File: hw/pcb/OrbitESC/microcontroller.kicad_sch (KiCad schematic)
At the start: 11 parts, among them J2 Micro_SD_Card_Det, J6 CAN1, J7 Serial1, SW1 Reset, SW2 Boot, SW3 Break, U1 MCP2551-I-SN, U2 AT25SF081-SSHD-X, U3 24LC128, U4 STM32F446ZCHx, X1 ECS-2520MV-240-BN

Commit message: Fill out majority of schematic
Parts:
- removed SW1: Reset, Button_Switch_SMD:SW_SPST_PTS810, symbol Switch:SW_Push
- removed SW2: Boot, Button_Switch_SMD:SW_SPST_PTS810, symbol Switch:SW_Push
- removed SW3: Break, Button_Switch_SMD:SW_SPST_PTS810, symbol Switch:SW_Push
- removed U1: MCP2551-I-SN, Package_SO:SOIC-8_3.9x4.9mm_P1.27mm, symbol Interface_CAN_LIN:MCP2551-I-SN
- added C33, C37, C38, C53: 2.2uF, Capacitor_SMD:C_0805_2012Metric, symbol Device:C
- added C34, C35, C36, C39, C40, C41, C42, C43, C44, C45, C46, C47, C48, C49, C50, C51, C52, C54, C55, C56: 100nF, Capacitor_SMD:C_0402_1005Metric, symbol Device:C
- added D10, D11, D8, D9: Yellow LED, Diode_SMD:D_0603_1608Metric, symbol Device:LED
- added D12, D13, D6, D7: 3.3V, Diode_SMD:D_MiniMELF, symbol Device:D_Zener
- added J10: ~, Connector_PinHeader_1.27mm:PinHeader_2x05_P1.27mm_Vertical, symbol Connector_Generic:Conn_02x05_Odd_Even
- added J8: Serial2, Connector_JST:JST_PH_B3B-PH-K_1x03_P2.00mm_Vertical, symbol Connector:Conn_01x03_Male
- added J9: CAN2, Connector_JST:JST_PH_B3B-PH-K_1x03_P2.00mm_Vertical, symbol Connector:Conn_01x03_Male
- added R58, R59, R60, R61, R64, R65, R66, R67, R68, R77, R78: 1.5k, Resistor_SMD:R_0402_1005Metric, symbol Device:R_US
- added R62, R63: 120, Resistor_SMD:R_0402_1005Metric, symbol Device:R_US
- added R69, R70, R71: 10k, Resistor_SMD:R_0402_1005Metric, symbol Device:R_US
- added R72, R73, R74, R75, R76: 39k, Resistor_SMD:R_0402_1005Metric, symbol Device:R_US
- added R80, R81, R82, R83: 100k, Resistor_SMD:R_0402_1005Metric, symbol Device:R_US
- added TP?: SDIO_CMD, TestPoint:TestPoint_Pad_D1.0mm, symbol Connector:TestPoint_Small
- added TP? (x2): TestPoint_Small, TestPoint:TestPoint_Pad_D1.0mm, symbol Connector:TestPoint_Small
- added U1, U10: TLE9250X, Package_SON:HVSON-8-1EP_3x3mm_P0.65mm_EP1.6x2.4mm, symbol CANTransciever:TLE9250X
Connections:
- net +3.3V: now also J2.4 (VDD), U2.3 (~{WP}/IO2), U2.7 (~{HOLD}/IO3), U2.8 (VCC), U3.8 (VCC), U4.C11 (VDDUSB), U4.C2 (VBAT), U4.D3 (VDD), U4.E5 (PDR_ON), U4.F10 (VDD), U4.F4 (VDD), U4.F5 (VDD), U4.F6 (VDD), U4.F7 (VDD), U4.F8 (VDD), U4.F9 (VDD), U4.G5 (VDD), U4.G6 (VDD), U4.G7 (VDD), X1.4 (VDD), C33.2, C34.2, C35.2, C36.2, C39.2, C40.2, C41.2, C42.2, C43.2, C44.2, C45.2, C46.2, C47.2, C48.2, C50.2, C51.2, C52.2, C53.2, C54.2, C55.2, C56.2, R64.2, R70.2, R71.2, R72.1, R73.1, R74.1, R75.1, R76.1, R77.2, R78.1, U1.5 (VIO), U10.5 (VIO)
- net +3.3VADC: now also U4.L1 (VREF+), U4.M1 (VDDA)
- net +5V: now also U1.3 (VCC), U10.3 (VCC)
- net USB_ENUM: now also U4.E12 (PA8); no longer U4.F12 (PC7)
- net GND: now reaches X1.2 (GND)
- net GND: now also J2.11 (SHIELD), J2.6 (VSS), J2.9 (DET_B), J6.2 (Pin_2), J7.3 (Pin_3), U2.4 (GND), U3.1 (A0), U3.2 (A1), U3.3 (A2), U3.4 (GND), U3.7 (WP), U4.D2 (VSS), U4.E6 (VSS), U4.E7 (VSS), U4.G10 (VSS), U4.G4 (VSS), U4.G8 (VSS), U4.H6 (VSS), U4.J1 (VSSA), U4.K1 (VREF-), C33.1, C34.1, C35.1, C36.1, C37.1, C38.1, C39.1, C40.1, C41.1, C42.1, C43.1, C44.1, C45.1, C46.1, C47.1, C48.1, C49.1, C50.1, C51.1, C52.1, C53.1, C54.1, C55.1, C56.1, D10.1 (K), D11.1 (K), D12.2 (A), D13.2 (A), D6.2 (A), D7.2 (A), D8.1 (K), D9.1 (K), J10.3 (Pin_3), J10.5 (Pin_5), J10.9 (Pin_9), J8.3 (Pin_3), J9.2 (Pin_2), R69.1, R80.1, R81.1, R82.2, R83.2, U1.2 (GND), U1.9 (PAD), U10.2 (GND), U10.9 (PAD)
- net OSC: now reaches X1.3 (OUT)
- net OSC: now also U4.D1 (PH0)
- net SDIO_DATA_2: now reaches J2.1 (DAT2)
- net SDIO_DATA_2: now also U4.B11 (PC10), R76.2
- net SDIO_CARD_DETECT: now reaches J2.10 (DET_A)
- net SDIO_CARD_DETECT: now also U4.D10 (PD1), C49.2, R72.2
- net SDIO_DATA_3: now reaches J2.2 (DAT3/CD)
- net SDIO_DATA_3: now also U4.B10 (PC11), R75.2
- net SDIO_CMD: now reaches J2.3 (CMD)
- net SDIO_CMD: now also U4.E9 (PD2), R71.1, TP?.1
- net SDIO_CLK: now reaches J2.5 (CLK)
- net SDIO_CLK: now also U4.C10 (PC12), TP?.1
- net SDIO_DATA_0: now reaches J2.7 (DAT0)
- net SDIO_DATA_0: now also U4.F11 (PC8), R73.2
- net SDIO_DATA_1: now reaches J2.8 (DAT1)
- net SDIO_DATA_1: now also U4.E11 (PC9), R74.2
- net HEARTBEAT_LED: now reaches U4.A1 (PC13)
- net JTAG_TDI: now reaches U4.A10 (PA15)
- net JTAG_TDI: now also J10.8 (Pin_8)
- net JTAG_TCLK: now reaches U4.A11 (PA14)
- net JTAG_TCLK: now also J10.4 (Pin_4)
- net JTAG_TMS: now reaches U4.A12 (PA13)
- net JTAG_TMS: now also J10.2 (Pin_2)
- net USER_BTN: now reaches U4.A2 (PE3)
- net ARMED_LED: now reaches U4.A4 (PE1)
- net CAN1_ACTV_LED: now reaches U4.A5 (PE0)
- net CAN1_ACTV_LED: now also R65.1
- net JTAG_TDO: now reaches U4.A7 (PB3)
- net JTAG_TDO: now also J10.6 (Pin_6)
- net SERIAL1_IN: now reaches U4.A8 (PD6)
- net SERIAL1_IN: now also R58.1, R82.1
- net STATUS_0_LED: now reaches U4.B2 (PE4)
- net STATUS_1_LED: now reaches U4.B3 (PE5)
- net STATUS_2_LED: now reaches U4.B4 (PE6)
- net CAN1_TXD: now reaches U4.B5 (PB9)
- net CAN1_TXD: now also U1.1 (TxD)
- net CAN2_RXD: now reaches U4.B6 (PB5)
- net CAN2_RXD: now also U10.4 (RxD)
- net CAN2_ACTV_LED: now reaches U4.B7 (PG15)
- net CAN2_ACTV_LED: now also R66.1
- net SERIAL1_ACTV_LED: now reaches U4.B8 (PG12)
- net SERIAL1_ACTV_LED: now also R67.1
- net SERIAL1_OUT: now reaches U4.B9 (PD5)
- net SERIAL1_OUT: now also R60.1, R80.2
- net EEPROM_SDA: now reaches U4.C3 (PF0)
- net EEPROM_SDA: now also U3.5 (SDA), R77.1
- net EEPROM_SCL: now reaches U4.C4 (PF1)
- net EEPROM_SCL: now also U3.6 (SCL), R78.2
- net CAN1_RXD: now reaches U4.C5 (PB8)
- net CAN1_RXD: now also U1.4 (RxD)
- net CAN2_TXD: now reaches U4.C6 (PB6)
- net CAN2_TXD: now also U10.1 (TxD)
- net SERIAL2_OUT: now reaches U4.C7 (PG14)
- net SERIAL2_OUT: now also R61.1, R81.2
- net USB_ACTV_LED: now reaches U4.D11 (PA10)
- net BOOT0: now reaches U4.D5 (BOOT0)
- net SERIAL2_ACTV_LED: now reaches U4.D7 (PG13)
- net SERIAL2_ACTV_LED: now also R68.1
- net TEMP_VA: now reaches U4.E2 (PF3)
- net SERIAL2_IN: now reaches U4.E8 (PG9)
- net SERIAL2_IN: now also R59.1, R83.1
- net nRESET: now reaches U4.F1 (NRST)
- net nRESET: now also J10.10 (Pin_10)
- net +3V3_VOLTAGE: now reaches U4.G1 (PF10)
- net TEMP_VB: now reaches U4.G2 (PF9)
- net at U4.G9 (VCAP_2): now also C38.2
- net +5V0_VOLTAGE: now reaches U4.H1 (PC0)
- net at U4.H5 (BYPASS_REG): now also R69.2
- net at U4.H7 (VCAP_1): now also C37.2
- net GATE_DRIVE_BH: now reaches U4.H8 (PE11)
- net INPUT_VOLTAGE: now reaches U4.J2 (PA0)
- net MOTOR_VA: now reaches U4.J3 (PA4)
- net BOOT1: now reaches U4.J5 (PB2)
- net GATE_DRIVE_BL: now reaches U4.J7 (PE10)
- net GATE_DRIVE_CL: now reaches U4.J8 (PE12)
- net MOTOR_IA: now reaches U4.K2 (PA1)
- net MOTOR_VB: now reaches U4.K3 (PA5)
- net GATE_DRIVE_AH: now reaches U4.K7 (PE9)
- net GATE_DRIVE_CH: now reaches U4.K8 (PE13)
- net NOR_MISO: now reaches U4.L11 (PB14)
- net NOR_MISO: now also U2.2 (SO/IO1)
- net NOR_MOSI: now reaches U4.L12 (PB15)
- net NOR_MOSI: now also U2.5 (SI/IO0)
- net MOTOR_IB: now reaches U4.L2 (PA2)
- net MOTOR_VC: now reaches U4.L3 (PA6)
- net GATE_DRIVE_AL: now reaches U4.L7 (PE8)
- net NOR_nCS: now reaches U4.M11 (PB12)
- net NOR_nCS: now also U2.1 (~{CS}), R70.1
- net NOR_SCK: now reaches U4.M12 (PB13)
- net NOR_SCK: now also U2.6 (SCK)
- net MOTOR_IC: now reaches U4.M2 (PA3)
- net TIM1_BREAK: now reaches U4.M8 (PE15)
- net at J7.1 (Pin_1): now also D6.1 (K), R60.2
- net at J7.2 (Pin_2): now also D12.1 (K), R58.2
- net at J6.1 (Pin_1): now also R62.2, U1.7 (CANH)
- net at J6.3 (Pin_3): now also R62.1, U1.6 (CANL)
- new net: J10.1 (Pin_1), R64.1
- new net: D7.1 (K), J8.1 (Pin_1), R61.2
- new net: D13.1 (K), J8.2 (Pin_2), R59.2
- new net: D8.2 (A), R65.2
- new net: D11.2 (A), R68.2
- new net: J9.3 (Pin_3), R63.1, U10.6 (CANL)
- new net: J9.1 (Pin_1), R63.2, U10.7 (CANH)
- new net: D10.2 (A), R67.2
- new net: D9.2 (A), R66.2
- no-connect marks 0 -> 4
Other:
- added sheet InputButton (input_button.kicad_sch)
- added sheet Status LEDs (status_leds.kicad_sch)
- sheet USBCircuitry ports: added ACTV_LED; removed none
- note added: "24MHz Oscillator"
- note added: "Enable Internal Regulator"
- note added: "Join at single point"
- note added: "Power Pins Decoupling"
- note added: "VDDUSB Decoupling"
- moved on the sheet: J2, J6, J7, U2, U3, X1

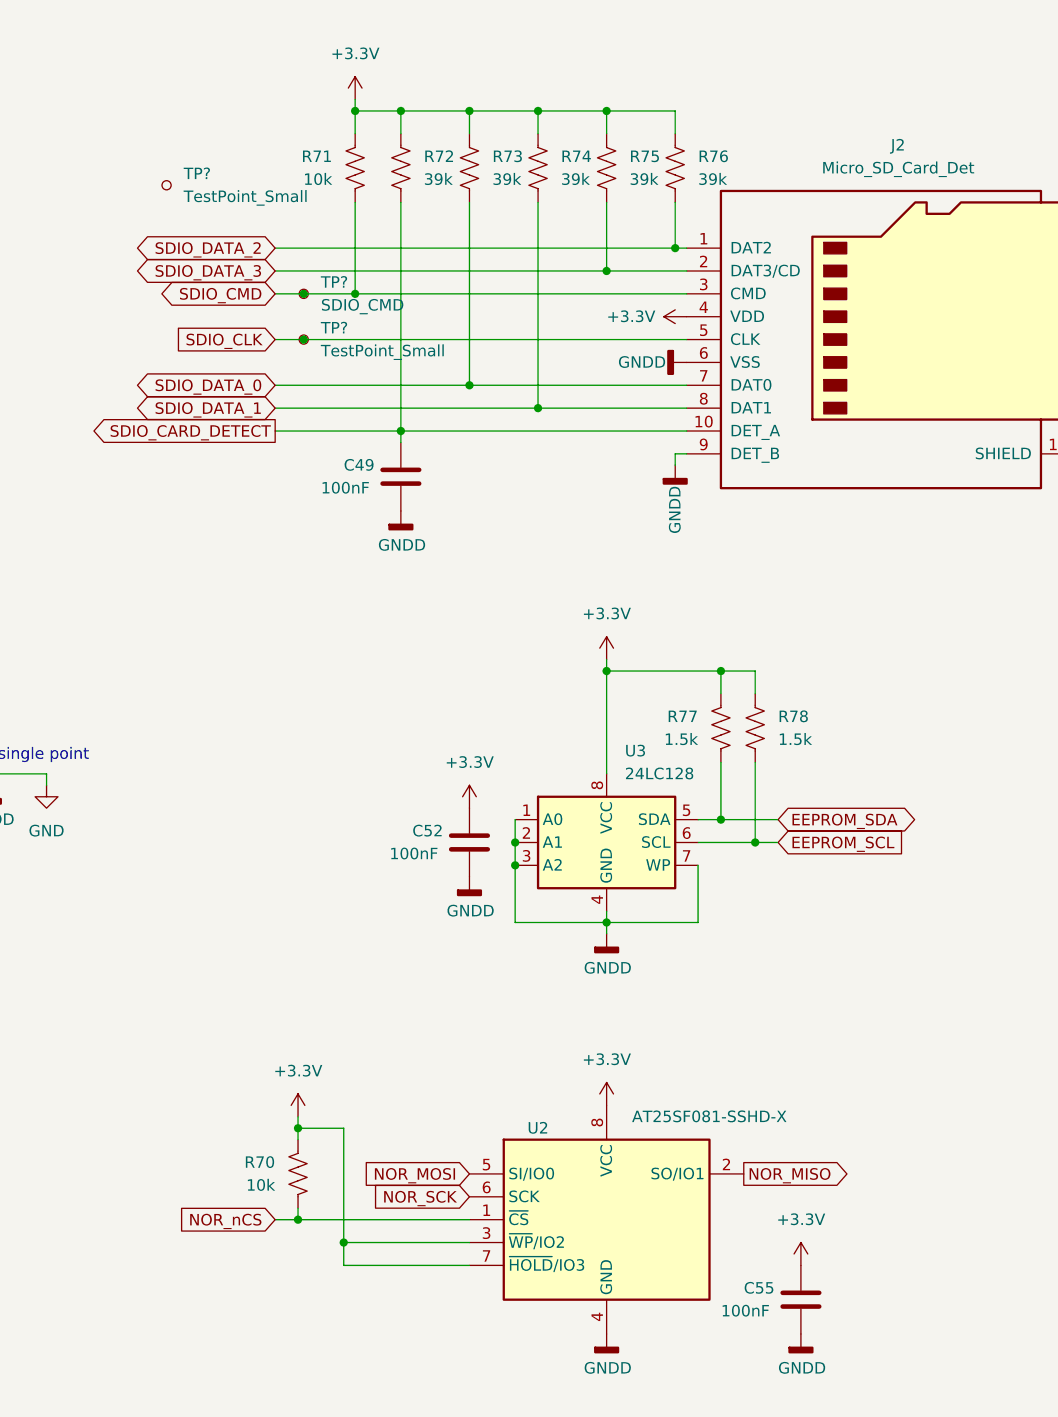
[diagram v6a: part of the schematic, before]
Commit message: Add test pads
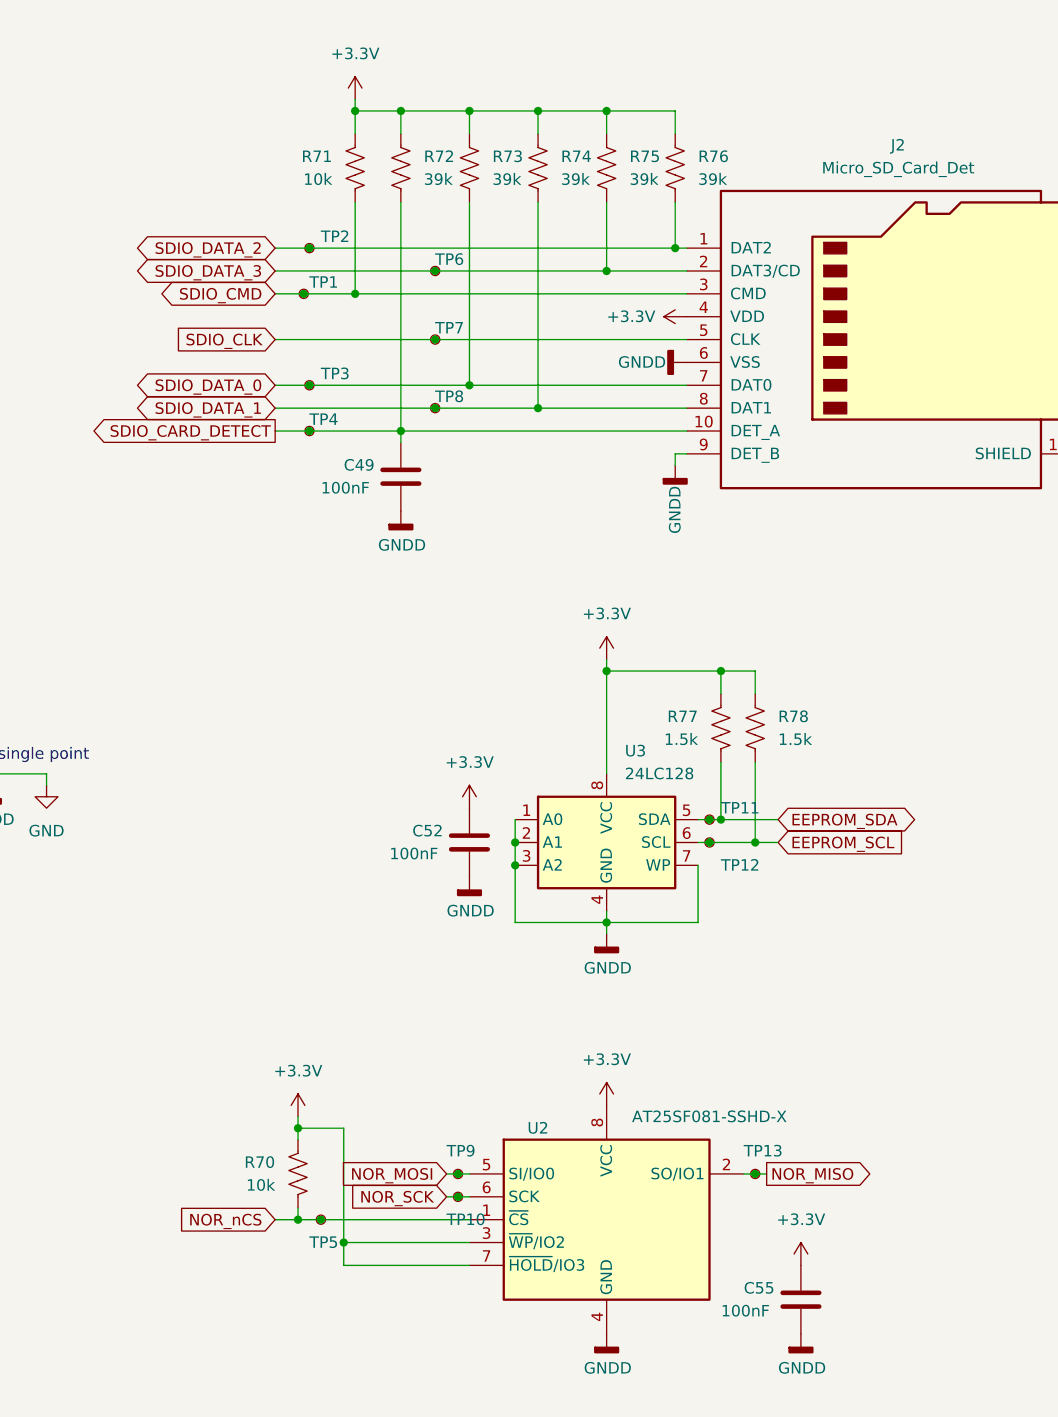
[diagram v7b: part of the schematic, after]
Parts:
- removed TP?: TestPoint_Small, TestPoint:TestPoint_Pad_D1.0mm, symbol Connector:TestPoint_Small
- added TP10: NOR_SCK, TestPoint:TestPoint_Pad_D1.0mm, symbol Connector:TestPoint_Small
- added TP11: EEPROM_SDA, TestPoint:TestPoint_Pad_D1.0mm, symbol Connector:TestPoint_Small
- added TP12: EEPROM_SCL, TestPoint:TestPoint_Pad_D1.0mm, symbol Connector:TestPoint_Small
- added TP13: NOR_MISO, TestPoint:TestPoint_Pad_D1.0mm, symbol Connector:TestPoint_Small
- added TP2: SDIO_DATA_2, TestPoint:TestPoint_Pad_D1.0mm, symbol Connector:TestPoint_Small
- added TP3: SDIO_DATA_0, TestPoint:TestPoint_Pad_D1.0mm, symbol Connector:TestPoint_Small
- added TP4: SDIO_CARD_DETECT, TestPoint:TestPoint_Pad_D1.0mm, symbol Connector:TestPoint_Small
- added TP5: NOR_nCS, TestPoint:TestPoint_Pad_D1.0mm, symbol Connector:TestPoint_Small
- added TP6: SDIO_DATA_3, TestPoint:TestPoint_Pad_D1.0mm, symbol Connector:TestPoint_Small
- added TP8: SDIO_DATA_1, TestPoint:TestPoint_Pad_D1.0mm, symbol Connector:TestPoint_Small
- added TP9: NOR_MOSI, TestPoint:TestPoint_Pad_D1.0mm, symbol Connector:TestPoint_Small
- TP7: renamed from TP?; value TestPoint_Small -> SDIO_CLK
- gave numbers to parts that had none: 1
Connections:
- net EEPROM_SCL: now also TP12.1
- net EEPROM_SDA: now also TP11.1
- net NOR_MISO: now also TP13.1
- net NOR_MOSI: now also TP9.1
- net NOR_SCK: now also TP10.1
- net NOR_nCS: now also TP5.1
- net SDIO_CARD_DETECT: now also TP4.1
- net SDIO_DATA_0: now also TP3.1
- net SDIO_DATA_1: now also TP8.1
- net SDIO_DATA_2: now also TP2.1
- net SDIO_DATA_3: now also TP6.1
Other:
- moved on the sheet: TP7

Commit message: Schematic checklist runthrough
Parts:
- J10: DigiKey (none) -> 609-3712-ND; Digikey 609-3712-ND -> (none); Mouser 649-221111-00010T4LF -> (none)
- J6, J7, J8, J9: DigiKey (none) -> A100035-ND
- U2: DigiKey (none) -> 1265-AT25SF081B-SSHD-B-ND
- U3: DigiKey (none) -> 24LC128T-E/MSCT-ND
- U4: DigiKey (none) -> 497-19011-ND; Digikey 497-19011-ND -> (none)
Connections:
- net FAULT_LED: now also U4.A3 (PE2)
- no-connect marks 4 -> 55
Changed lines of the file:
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@@
   )
   (no_connect (at 232.41 124.46))
+  (no_connect (at 166.37 114.3))
+  (no_connect (at 166.37 134.62))
+  (no_connect (at 166.37 132.08))
+  (no_connect (at 166.37 129.54))
+  (no_connect (at 166.37 139.7))
+  (no_connect (at 166.37 142.24))
+  (no_connect (at 166.37 127))
+  (no_connect (at 166.37 124.46))
+  (no_connect (at 166.37 121.92))
+  (no_connect (at 166.37 119.38))
+  (no_connect (at 166.37 116.84))
+  (no_connect (at 166.37 162.56))
+  (no_connect (at 166.37 167.64))
+  (no_connect (at 166.37 170.18))
+  (no_connect (at 166.37 172.72))
+  (no_connect (at 166.37 175.26))
+  (no_connect (at 166.37 177.8))
+  (no_connect (at 166.37 185.42))
+  (no_connect (at 166.37 187.96))
+  (no_connect (at 166.37 190.5))
   (no_connect (at 109.22 39.37))
+  (no_connect (at 166.37 218.44))
+  (no_connect (at 166.37 236.22))
+  (no_connect (at 232.41 238.76))
+  (no_connect (at 232.41 236.22))
+  (no_connect (at 232.41 233.68))
+  (no_connect (at 232.41 231.14))
+  (no_connect (at 232.41 228.6))
+  (no_connect (at 232.41 226.06))
+  (no_connect (at 232.41 139.7))
+  (no_connect (at 232.41 142.24))
+  (no_connect (at 232.41 132.08))
+  (no_connect (at 232.41 210.82))
+  (no_connect (at 232.41 208.28))
+  (no_connect (at 232.41 200.66))
+  (no_connect (at 232.41 223.52))
+  (no_connect (at 232.41 220.98))
+  (no_connect (at 232.41 218.44))
+  (no_connect (at 232.41 195.58))
+  (no_connect (at 232.41 193.04))
+  (no_connect (at 232.41 175.26))
+  (no_connect (at 232.41 172.72))
+  (no_connect (at 232.41 170.18))
+  (no_connect (at 232.41 167.64))
+  (no_connect (at 232.41 165.1))
+  (no_connect (at 232.41 162.56))
+  (no_connect (at 232.41 160.02))
+  (no_connect (at 232.41 116.84))
+  (no_connect (at 232.41 114.3))
+  (no_connect (at 232.41 88.9))
+  (no_connect (at 166.37 193.04))
+  (no_connect (at 166.37 195.58))
   (no_connect (at 39.37 36.83))
   (no_connect (at 166.37 109.22))
@@
     )
   )
+  (global_label "FAULT_LED" (shape output) (at 166.37 205.74 180) (fields_autoplaced)
+    (effects (font (size 1.27 1.27)) (justify right))
+    (property "Intersheet References" "${INTERSHEET_REFS}" (id 0) (at 154.0388 205.8194 0)
+      (effects (font (size 1.27 1.27)) (justify right) hide)
+    )
+  )
   (global_label "SERIAL2_OUT" (shape output) (at 166.37 149.86 180) (fields_autoplaced)
     (effects (font (size 1.27 1.27)) (justify right))
@@
       (effects (font (size 1.27 1.27)) hide)
     )
-    (property "Mouser" "649-221111-00010T4LF" (id 4) (at 114.3 36.83 0)
-      (effects (font (size 1.27 1.27)) hide)
-    )
-    (property "PartNumber" "" (id 5) (at 114.3 36.83 0)
-      (effects (font (size 1.27 1.27)) hide)
-    )
-    (property "Digikey" "609-3712-ND" (id 6) (at 114.3 36.83 0)
+    (property "DigiKey" "609-3712-ND" (id 6) (at 114.3 36.83 0)
       (effects (font (size 1.27 1.27)) hide)
     )
@@
       (effects (font (size 1.27 1.27)) hide)
     )
+    (property "DigiKey" "A100035-ND" (id 4) (at 92.71 264.16 0)
+      (effects (font (size 1.27 1.27)) hide)
+    )
     (pin "1")
     (pin "2")
@@
       (effects (font (size 1.27 1.27)) hide)
     )
-    (property "Digikey" "497-19011-ND" (id 4) (at 199.39 154.94 0)
+    (property "DigiKey" "497-19011-ND" (id 4) (at 199.39 154.94 0)
       (effects (font (size 1.27 1.27)) hide)
     )
@@
       (effects (font (size 1.27 1.27)) hide)
     )
+    (property "DigiKey" "24LC128T-E/MSCT-ND" (id 4) (at 337.82 166.37 0)
+      (effects (font (size 1.27 1.27)) hide)
+    )
     (pin "1")
     (pin "2")
@@
       (effects (font (size 1.27 1.27)) hide)
     )
-    (property "Datasheet" "https://www.adestotech.com/wp-content/uploads/DS-AT25SF081_045.pdf" (id 3) (at 337.82 208.28 0)
+    (property "Datasheet" "https://www.mouser.com/datasheet/2/590/DS-AT25SF081_045-1385733.pdf" (id 3) (at 337.82 208.28 0)
+      (effects (font (size 1.27 1.27)) hide)
+    )
+    (property "DigiKey" "1265-AT25SF081B-SSHD-B-ND" (id 4) (at 337.82 208.28 0)
       (effects (font (size 1.27 1.27)) hide)
     )
@@
       (effects (font (size 1.27 1.27)) hide)
     )
+    (property "DigiKey" "A100035-ND" (id 4) (at 96.52 196.85 0)
+      (effects (font (size 1.27 1.27)) hide)
+    )
     (pin "1")
     (pin "2")
@@
       (effects (font (size 1.27 1.27)) hide)
     )
+    (property "DigiKey" "A100035-ND" (id 4) (at 92.71 231.14 0)
+      (effects (font (size 1.27 1.27)) hide)
+    )
     (pin "1")
     (pin "2")
@@
       (effects (font (size 1.27 1.27)) hide)
     )
+    (property "DigiKey" "A100035-ND" (id 4) (at 96.52 157.48 0)
+      (effects (font (size 1.27 1.27)) hide)
+    )
